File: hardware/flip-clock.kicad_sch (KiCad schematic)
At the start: 13 parts, among them J1 Screw_Terminal_01x02, J2 Conn_01x04, U1 WeMos_D1_mini

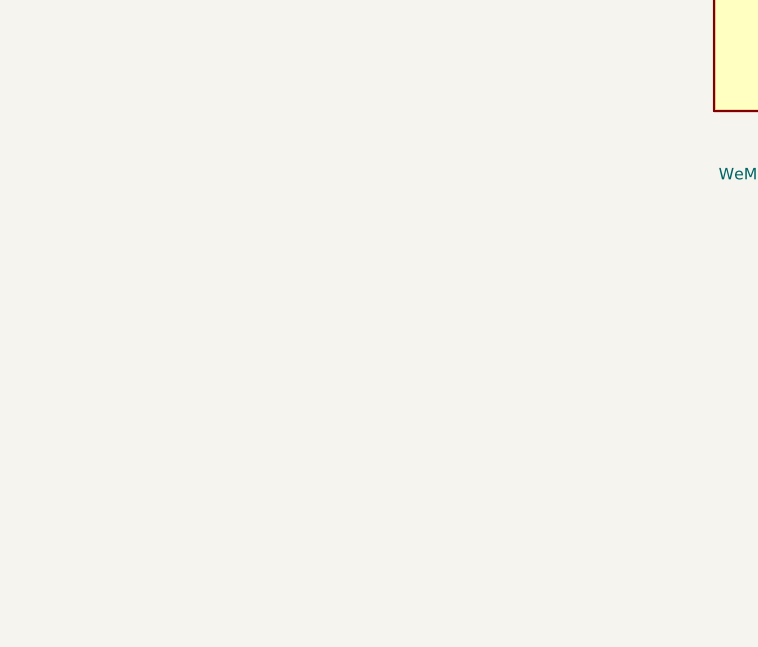
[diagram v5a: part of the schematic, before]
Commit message: second PCB-Part for IR
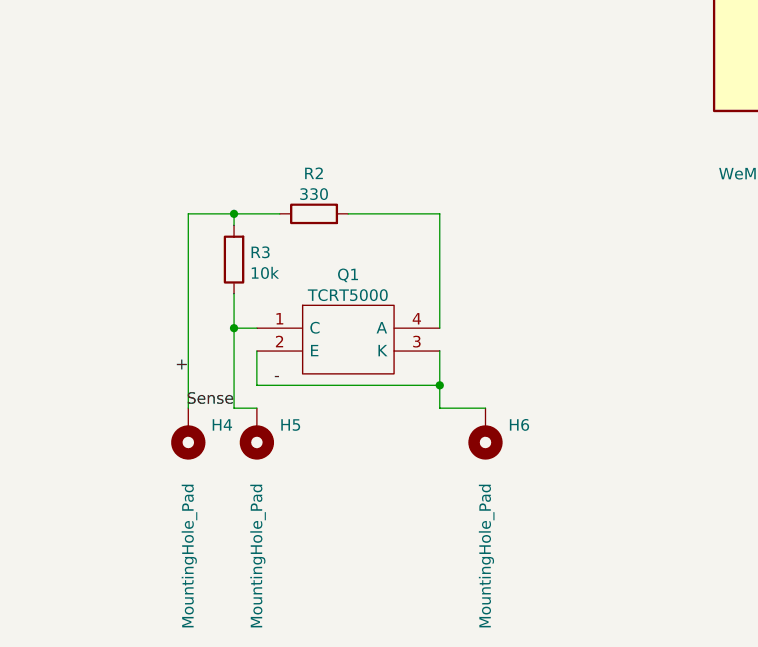
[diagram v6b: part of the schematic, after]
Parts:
- added H4, H5, H6: MountingHole_Pad, Connector_Wire:SolderWirePad_1x01_SMD_1x2mm, symbol Mechanical:MountingHole_Pad
- added Q1: TCRT5000, KiCad:TCRT5000, symbol TCRT5000:TCRT5000
- added R2: 330, Resistor_SMD:R_0805_2012Metric, symbol Device:R
- added R3: 10k, Resistor_SMD:R_0805_2012Metric, symbol Device:R
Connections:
- new net: Q1.4 (A), R2.2
- new net +: H4.1, R2.1, R3.2
- new net -: H6.1, Q1.2 (E), Q1.3 (K)
- new net Sense: H5.1, Q1.1 (C), R3.1
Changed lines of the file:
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@@
 (kicad_sch (version 20210406) (generator eeschema)
   (paper "A4")
+  (junction (at 43.18 106.68) (diameter 0.9144) (color 0 0 0 0))
+  (junction (at 43.18 119.38) (diameter 0.9144) (color 0 0 0 0))
+  (junction (at 66.04 125.73) (diameter 0.9144) (color 0 0 0 0))
   (junction (at 118.11 33.02) (diameter 0.9144) (color 0 0 0 0))
   (junction (at 118.11 40.64) (diameter 0.9144) (color 0 0 0 0))
@@
     (stroke (width 0) (type solid) (color 0 0 0 0))
   )
+  (wire (pts (xy 38.1 106.68) (xy 43.18 106.68))
+    (stroke (width 0) (type solid) (color 0 0 0 0))
+  )
+  (wire (pts (xy 38.1 128.27) (xy 38.1 106.68))
+    (stroke (width 0) (type solid) (color 0 0 0 0))
+  )
+  (wire (pts (xy 43.18 106.68) (xy 43.18 107.95))
+    (stroke (width 0) (type solid) (color 0 0 0 0))
+  )
+  (wire (pts (xy 43.18 106.68) (xy 48.26 106.68))
+    (stroke (width 0) (type solid) (color 0 0 0 0))
+  )
+  (wire (pts (xy 43.18 115.57) (xy 43.18 119.38))
+    (stroke (width 0) (type solid) (color 0 0 0 0))
+  )
+  (wire (pts (xy 43.18 119.38) (xy 45.72 119.38))
+    (stroke (width 0) (type solid) (color 0 0 0 0))
+  )
+  (wire (pts (xy 43.18 128.27) (xy 43.18 119.38))
+    (stroke (width 0) (type solid) (color 0 0 0 0))
+  )
+  (wire (pts (xy 45.72 121.92) (xy 45.72 125.73))
+    (stroke (width 0) (type solid) (color 0 0 0 0))
+  )
+  (wire (pts (xy 45.72 125.73) (xy 66.04 125.73))
+    (stroke (width 0) (type solid) (color 0 0 0 0))
+  )
+  (wire (pts (xy 45.72 128.27) (xy 43.18 128.27))
+    (stroke (width 0) (type solid) (color 0 0 0 0))
+  )
+  (wire (pts (xy 55.88 106.68) (xy 66.04 106.68))
+    (stroke (width 0) (type solid) (color 0 0 0 0))
+  )
   (wire (pts (xy 62.23 29.21) (xy 71.12 29.21))
     (stroke (width 0) (type solid) (color 0 0 0 0))
@@
     (stroke (width 0) (type solid) (color 0 0 0 0))
   )
+  (wire (pts (xy 66.04 106.68) (xy 66.04 119.38))
+    (stroke (width 0) (type solid) (color 0 0 0 0))
+  )
+  (wire (pts (xy 66.04 121.92) (xy 66.04 125.73))
+    (stroke (width 0) (type solid) (color 0 0 0 0))
+  )
+  (wire (pts (xy 66.04 125.73) (xy 66.04 128.27))
+    (stroke (width 0) (type solid) (color 0 0 0 0))
+  )
+  (wire (pts (xy 66.04 128.27) (xy 71.12 128.27))
+    (stroke (width 0) (type solid) (color 0 0 0 0))
+  )
   (wire (pts (xy 71.12 26.67) (xy 71.12 29.21))
     (stroke (width 0) (type solid) (color 0 0 0 0))
@@
   (wire (pts (xy 177.8 63.5) (xy 177.8 64.77))
     (stroke (width 0) (type solid) (color 0 0 0 0))
+  )
+  (label "+" (at 38.1 124.46 180)
+    (effects (font (size 1.27 1.27)) (justify right bottom))
+  )
+  (label "Sense" (at 43.18 128.27 180)
+    (effects (font (size 1.27 1.27)) (justify right bottom))
+  )
+  (label "-" (at 48.26 125.73 180)
+    (effects (font (size 1.27 1.27)) (justify right bottom))
   )
   (label "AC2" (at 66.04 31.75 0)
@@
     )
   )
+  (symbol (lib_id "Device:R") (at 43.18 111.76 180) (unit 1)
+    (in_bom yes) (on_board yes) (fields_autoplaced)
+    (property "Reference" "R3" (id 0) (at 44.9581 110.9991 0)
+      (effects (font (size 1.27 1.27)) (justify right))
+    )
+    (property "Value" "10k" (id 1) (at 44.9581 113.2978 0)
+      (effects (font (size 1.27 1.27)) (justify right))
+    )
+    (property "Footprint" "Resistor_SMD:R_0805_2012Metric" (id 2) (at 44.958 111.76 90)
+      (effects (font (size 1.27 1.27)) hide)
+    )
+    (property "Datasheet" "~" (id 3) (at 43.18 111.76 0)
+      (effects (font (size 1.27 1.27)) hide)
+    )
+    (pin "1")
+    (pin "2")
+  )
+  (symbol (lib_id "Device:R") (at 52.07 106.68 90) (unit 1)
+    (in_bom yes) (on_board yes) (fields_autoplaced)
+    (property "Reference" "R2" (id 0) (at 52.07 102.2308 90))
+    (property "Value" "330" (id 1) (at 52.07 104.5295 90))
+    (property "Footprint" "Resistor_SMD:R_0805_2012Metric" (id 2) (at 52.07 108.458 90)
+      (effects (font (size 1.27 1.27)) hide)
+    )
+    (property "Datasheet" "~" (id 3) (at 52.07 106.68 0)
+      (effects (font (size 1.27 1.27)) hide)
+    )
+    (pin "1")
+    (pin "2")
+  )
   (symbol (lib_id "Device:R") (at 110.49 36.83 0) (unit 1)
     (in_bom yes) (on_board yes) (fields_autoplaced)
@@
     )
     (property "Datasheet" "~" (id 3) (at 27.94 38.1 0)
+      (effects (font (size 1.27 1.27)) hide)
+    )
+    (pin "1")
+  )
+  (symbol (lib_id "Mechanical:MountingHole_Pad") (at 38.1 130.81 180) (unit 1)
+    (in_bom yes) (on_board yes)
+    (property "Reference" "H4" (id 0) (at 40.6401 130.1761 0)
+      (effects (font (size 1.27 1.27)) (justify right))
+    )
+    (property "Value" "MountingHole_Pad" (id 1) (at 38.1001 152.7948 90)
+      (effects (font (size 1.27 1.27)) (justify right))
+    )
+    (property "Footprint" "Connector_Wire:SolderWirePad_1x01_SMD_1x2mm" (id 2) (at 38.1 130.81 0)
+      (effects (font (size 1.27 1.27)) hide)
+    )
+    (property "Datasheet" "~" (id 3) (at 38.1 130.81 0)
+      (effects (font (size 1.27 1.27)) hide)
+    )
+    (pin "1")
+  )
+  (symbol (lib_id "Mechanical:MountingHole_Pad") (at 45.72 130.81 180) (unit 1)
+    (in_bom yes) (on_board yes)
+    (property "Reference" "H5" (id 0) (at 48.2601 130.1761 0)
+      (effects (font (size 1.27 1.27)) (justify right))
+    )
+    (property "Value" "MountingHole_Pad" (id 1) (at 45.7201 152.7948 90)
+      (effects (font (size 1.27 1.27)) (justify right))
+    )
+    (property "Footprint" "Connector_Wire:SolderWirePad_1x01_SMD_1x2mm" (id 2) (at 45.72 130.81 0)
+      (effects (font (size 1.27 1.27)) hide)
+    )
+    (property "Datasheet" "~" (id 3) (at 45.72 130.81 0)
+      (effects (font (size 1.27 1.27)) hide)
+    )
+    (pin "1")
+  )
+  (symbol (lib_id "Mechanical:MountingHole_Pad") (at 71.12 130.81 180) (unit 1)
+    (in_bom yes) (on_board yes)
+    (property "Reference" "H6" (id 0) (at 73.6601 130.1761 0)
+      (effects (font (size 1.27 1.27)) (justify right))
+    )
+    (property "Value" "MountingHole_Pad" (id 1) (at 71.1201 152.7948 90)
+      (effects (font (size 1.27 1.27)) (justify right))
+    )
+    (property "Footprint" "Connector_Wire:SolderWirePad_1x01_SMD_1x2mm" (id 2) (at 71.12 130.81 0)
+      (effects (font (size 1.27 1.27)) hide)
+    )
+    (property "Datasheet" "~" (id 3) (at 71.12 130.81 0)
       (effects (font (size 1.27 1.27)) hide)
     )
@@
     (property "Datasheet" "~" (id 3) (at 128.27 35.56 0)
       (effects (font (size 1.27 1.27)) hide)
+    )
+    (pin "1")
+    (pin "2")
+    (pin "3")
+    (pin "4")
+  )
+  (symbol (lib_id "TCRT5000:TCRT5000") (at 45.72 119.38 0) (unit 1)
+    (in_bom yes) (on_board yes) (fields_autoplaced)
+    (property "Reference" "Q1" (id 0) (at 55.88 113.4576 0))
+    (property "Value" "TCRT5000" (id 1) (at 55.88 115.7563 0))
+    (property "Footprint" "KiCad:TCRT5000" (id 2) (at 62.23 116.84 0)
+      (effects (font (size 1.27 1.27)) (justify left) hide)
+    )
+    (property "Datasheet" "http://www.vishay.com/docs/83760/tcrt5000.pdf" (id 3) (at 62.23 119.38 0)
+      (effects (font (size 1.27 1.27)) (justify left) hide)
+    )
+    (property "Description" "VISHAY - TCRT5000. - SENSOR, OPTICAL, TRANSISTOR O/P" (id 4) (at 62.23 121.92 0)
+      (effects (font (size 1.27 1.27)) (justify left) hide)
+    )
+    (property "Height" "6.8" (id 5) (at 62.23 124.46 0)
+      (effects (font (size 1.27 1.27)) (justify left) hide)
+    )
+    (property "Manufacturer_Name" "Vishay" (id 6) (at 62.23 127 0)
+      (effects (font (size 1.27 1.27)) (justify left) hide)
+    )
+    (property "Manufacturer_Part_Number" "TCRT5000" (id 7) (at 62.23 129.54 0)
+      (effects (font (size 1.27 1.27)) (justify left) hide)
+    )
+    (property "Mouser Part Number" "782-TCRT5000" (id 8) (at 62.23 132.08 0)
+      (effects (font (size 1.27 1.27)) (justify left) hide)
+    )
+    (property "Mouser Price/Stock" "https://www.mouser.co.uk/ProductDetail/Vishay-Semiconductors/TCRT5000/?qs=glpcD2KT6uaaYldHGIIt5g%3D%3D" (id 9) (at 62.23 134.62 0)
+      (effects (font (size 1.27 1.27)) (justify left) hide)
+    )
+    (property "Arrow Part Number" "TCRT5000" (id 10) (at 62.23 137.16 0)
+      (effects (font (size 1.27 1.27)) (justify left) hide)
+    )
+    (property "Arrow Price/Stock" "https://www.arrow.com/en/products/tcrt5000/vishay" (id 11) (at 62.23 139.7 0)
+      (effects (font (size 1.27 1.27)) (justify left) hide)
     )
     (pin "1")
@@
       (reference "H3") (unit 1) (value "MountingHole") (footprint "MountingHole:MountingHole_3.2mm_M3_Pad")
     )
+    (path "/a81be5d6-faee-4193-969a-6fa361cff4ab"
+      (reference "H4") (unit 1) (value "MountingHole_Pad") (footprint "Connector_Wire:SolderWirePad_1x01_SMD_1x2mm")
+    )
+    (path "/d9de179d-e38d-4330-9e45-64d88705ef74"
+      (reference "H5") (unit 1) (value "MountingHole_Pad") (footprint "Connector_Wire:SolderWirePad_1x01_SMD_1x2mm")
+    )
+    (path "/8b564c2b-74b2-430b-b950-9c8acf122b5f"
+      (reference "H6") (unit 1) (value "MountingHole_Pad") (footprint "Connector_Wire:SolderWirePad_1x01_SMD_1x2mm")
+    )
     (path "/f713f965-e52a-49ca-82fb-31c7d4eb52c8"
       (reference "H-1A1") (unit 1) (value "MountingHole_Pad") (footprint "Connector_Wire:SolderWire-0.1sqmm_1x01_D0.4mm_OD1mm")
@@
       (reference "PS1") (unit 1) (value "HLK-PM01") (footprint "Converter_ACDC:Converter_ACDC_HiLink_HLK-PMxx")
     )
+    (path "/d192fe88-3d33-4e84-a776-21ebe6bb38dc"
+      (reference "Q1") (unit 1) (value "TCRT5000") (footprint "KiCad:TCRT5000")
+    )
     (path "/58bce13c-d699-4461-a4ab-97430eb06ca1"
       (reference "R1") (unit 1) (value "4k7") (footprint "Resistor_SMD:R_0805_2012Metric")
     )
+    (path "/5652473f-51c5-4709-afb9-0e50a9e46c96"
+      (reference "R2") (unit 1) (value "330") (footprint "Resistor_SMD:R_0805_2012Metric")
+    )
+    (path "/8712bf73-147b-43c1-b686-4964febb13cd"
+      (reference "R3") (unit 1) (value "10k") (footprint "Resistor_SMD:R_0805_2012Metric")
+    )
     (path "/967d53ac-169d-48b6-a5fc-633424bf7271"
